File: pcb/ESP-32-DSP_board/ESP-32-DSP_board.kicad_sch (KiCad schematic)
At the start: 65 parts, among them J1 USB_C_Receptacle_USB2.0, J10 Conn_01x01_Pin, J11 Conn_01x01_Pin, J2 Conn_01x04_Pin, J3 Conn_01x04_Pin, J4 Conn_01x07_Pin, J5 Conn_01x07_Pin, J6 Conn_01x01_Pin, J7 Conn_01x01_Pin, J8 Conn_01x01_Pin, J9 Conn_01x01_Pin, Q1 BC847, Q2 BC847, U1 AZ1117IH-3.3, U2 ESP32-WROOM-32UE-N8, U3 USBLC6-2P6, U4 CP2104, U5 ADS8688

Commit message: ESP32-S3 version of dsp board with SD-card and DAC added
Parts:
- removed C11: 4.7u, Capacitor_SMD:C_0603_1608Metric, symbol Device:C
- removed C5: 100n, Capacitor_SMD:C_0402_1005Metric, symbol Device:C
- removed J10, J11, J6, J7, J8, J9: Conn_01x01_Pin, Connector_PinSocket_2.00mm:PinSocket_1x01_P2.00mm_Vertical, symbol Connector:Conn_01x01_Pin
- removed J2, J3: Conn_01x04_Pin, Connector_PinHeader_2.00mm:PinHeader_1x04_P2.00mm_Horizontal, symbol Connector:Conn_01x04_Pin
- removed J4, J5: Conn_01x07_Pin, Connector_PinSocket_2.00mm:PinSocket_1x07_P2.00mm_Vertical, symbol Connector:Conn_01x07_Pin
- removed Q1, Q2: BC847, Package_TO_SOT_SMD:SOT-23, symbol Transistor_BJT:BC847
- removed R10 (x3): 10k, Resistor_SMD:R_0402_1005Metric, symbol Device:R_Small
- removed R10 (x3): 4.7k, Resistor_SMD:R_0402_1005Metric, symbol Device:R_Small
- removed U2: ESP32-WROOM-32UE-N8, RF_Module:ESP32-WROOM-32U, symbol RF_Module:ESP32-WROOM-32U
- removed U4: CP2104, Package_DFN_QFN:QFN-24-1EP_4x4mm_P0.5mm_EP2.6x2.6mm, symbol Interface_USB:CP2104
- added C27, C28: 3.3p, Capacitor_SMD:C_0402_1005Metric, symbol Device:C
- added C29: 10u, Capacitor_SMD:C_0603_1608Metric, symbol Device:C
- added C30: 1u, Capacitor_SMD:C_0603_1608Metric, symbol Device:C
- added C31, C32, C36: 100n, Capacitor_SMD:C_0402_1005Metric, symbol Device:C
- added C33, C34: 12p, Capacitor_SMD:C_0402_1005Metric, symbol Device:C
- added C5: 250u, Capacitor_THT:CP_Radial_D5.0mm_P2.50mm, symbol Device:C_Polarized
- added J12: Conn_Coaxial, Connector_Coaxial:U.FL_Hirose_U.FL-R-SMT-1_Vertical, symbol Connector:Conn_Coaxial
- added J2: Conn_01x10_Pin, Connector_PinHeader_2.54mm:PinHeader_1x10_P2.54mm_Vertical, symbol Connector:Conn_01x10_Pin
- added J5: SD_Card, Connector_Card:microSD_HC_Hirose_DM3D-SF, symbol Connector:SD_Card
- added J6: AudioJack2_Ground, Connector_Audio:Jack_3.5mm_CUI_SJ-3523-SMT_Horizontal, symbol Connector_Audio:AudioJack2_Ground
- added L1, L2, L4: 2.2n, Inductor_SMD:L_0603_1608Metric, symbol Device:L
- added R13: 10k, Resistor_SMD:R_0402_1005Metric, symbol Device:R
- added R14: 10, Resistor_SMD:R_0805_2012Metric, symbol Device:R
- added RV1, RV2: R_Potentiometer, Potentiometer_SMD:Potentiometer_ACP_CA6-VSMD_Vertical, symbol Device:R_Potentiometer
- added U2: AD5689BRUZ, Package_SO:TSSOP-16_4.4x5mm_P0.65mm, symbol Analog_DAC:AD5689BRUZ
- added U4: LM386, Package_SO:SOIC-8_3.9x4.9mm_P1.27mm, symbol Amplifier_Audio:LM386
- added U6: ESP32-S3FH4R2, Package_DFN_QFN:QFN-56-1EP_7x7mm_P0.4mm_EP5.6x5.6mm, symbol PCM_Espressif:ESP32-S3
- added Y1: 40MHz, Crystal:Crystal_SMD_3225-4Pin_3.2x2.5mm, symbol Device:Crystal_GND23
- C1: footprint Capacitor_SMD:C_0805_2012Metric -> Capacitor_SMD:C_0402_1005Metric
- C10: value 4.7u -> 10u
- C7: value 22u -> 10u; footprint Capacitor_SMD:C_0805_2012Metric -> Capacitor_SMD:C_0603_1608Metric
- C8: value 1u -> 10u; footprint Capacitor_SMD:C_0402_1005Metric -> Capacitor_SMD:C_0603_1608Metric
- C9: footprint Capacitor_SMD:C_0402_1005Metric -> Capacitor_SMD:C_0603_1608Metric
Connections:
- net +3.3V: now also C29.1, C30.1, C31.1, J5.4 (VDD), L2.1, R13.1, U2.1 (VREF), U2.10 (GAIN), U2.11 (VLOGIC), U2.15 (~{RESET}), U2.5 (VDD), U2.9 (~{LDAC}), U6.2 (VDD3P3), U6.20 (VDD3P3_RTC), U6.3 (VDD3P3), U6.46 (VDD3P3_CPU), U6.55 (VDDA), U6.56 (VDDA); no longer C7.1
- net ADC_A0: now also J2.3 (Pin_3)
- net ADC_A1: now also J2.4 (Pin_4)
- net ADC_A2: now also J2.5 (Pin_5)
- net ADC_A3: now also J2.6 (Pin_6)
- net ADC_A4: now also J2.7 (Pin_7)
- net ADC_A5: now also J2.8 (Pin_8)
- net ADC_A6: now also J2.1 (Pin_1)
- net ADC_A7: now also J2.2 (Pin_2)
- net ADC_CS: now also U6.9 (GPIO4/ADC1_CH3)
- net ADC_MISO: now also U6.8 (GPIO3/ADC1_CH2)
- net ADC_MOSI: now also U6.7 (GPIO2/ADC1_CH1)
- net ADC_SCLK: now also U6.10 (GPIO5/ADC1_CH4)
- net EN: now also U6.4 (CHIP_PU/RESET); no longer C8.1
- net GND: now also C27.2, C28.2, C29.2, C30.2, C31.2, C32.2, C33.1, C34.1, C36.2, J12.2 (Ext), J5.3 (VSS), J5.6 (VSS), J6.G, U2.16 (RSTSEL), U2.4 (GND), U6.57 (GND), Y1.2, Y1.4; no longer C7.2, C8.2, J1.S1 (SHIELD)
- net GNDA: now also C8.1, J2.9 (Pin_9), RV1.3, RV2.3, U4.2 (-), U4.4 (GND)
- net IO0: now also U6.5 (GPIO0/BOOT)
- net IO16: now also U6.22 (GPIO16/ADC2_CH5/XTAL_32K_N)
- net IO17: now also U6.23 (GPIO17/ADC2_CH6)
- net IO18: now also U6.24 (GPIO18/ADC2_CH7)
- net IO21: now also U6.27 (GPIO21)
- net RX: now also U6.50 (U0RXD/PROG/GPIO44)
- net TX: now also U6.49 (U0TXD/PROG/GPIO43)
- net USB_D+: now also U6.26 (GPIO20/USB_D+/ADC2_CH9)
- net USB_D-: now also U6.25 (GPIO19/USB_D-/ADC2_CH8)
- net VBUS renamed +5V
- net +5V: now also J2.10 (Pin_10), L4.1, U4.6 (V+); no longer C2.1, U1.3 (VI), U3.5 (VBUS)
- new net: C32.1, L2.2
- new net: C2.1, C36.1, L4.2, U1.3 (VI), U3.5 (VBUS)
- new net: C28.1, J12.1 (In), L1.1
- new net: C27.1, L1.2, U6.1 (LNA_IN/RF)
- new net: C33.2, U6.53 (XTAL_N), Y1.3
- new net: R14.1, U6.54 (XTAL_P)
- new net: RV2.1, U4.1 (GAIN)
- new net: C7.2, RV2.2
- new net: C34.2, R14.2, Y1.1
- new net: C5.1, U4.5
- new net: C5.2, J6.S, J6.T
- new net: C7.1, U4.8 (GAIN)
- new net: RV1.1, U2.3 (VOUTA)
- new net: RV1.2, U4.3 (+)
- new net: C8.2, U4.7 (BYPASS)
- new net DAC_MISO: U2.14 (SDIN), U6.15 (GPIO10/ADC1_CH9)
- new net DAC_MOSI: U2.8 (SDO), U6.18 (GPIO13/ADC2_CH2)
- new net DAC_SCLK: U2.12 (SCLK), U6.17 (GPIO12/ADC2_CH1)
- new net DAC_SYNC: U2.13 (~{SYNC}), U6.16 (GPIO11/ADC2_CH0)
- new net IO1: U6.6 (GPIO1/ADC1_CH0)
- new net IO14: U6.19 (GPIO14/ADC2_CH3)
- new net IO15: U6.21 (GPIO15/ADC2_CH4/XTAL_32K_P)
- new net IO38: U6.43 (GPIO38)
- new net IO39: U6.44 (MTCK/JTAG/GPIO39)
- new net IO40: U6.45 (MTDO/JTAG/GPIO40)
- new net IO41: U6.47 (MTDI/JTAG/GPIO41)
- new net IO42: U6.48 (MTMS/JTAG/GPIO42)
- new net IO45: R13.2, U6.51 (GPIO45)
- new net IO46: U6.52 (GPIO46)
- new net IO47: U6.37 (SPICLK_P/GPIO47)
- new net IO48: U6.36 (SPICLK_N/GPIO48)
- new net SD_CS: J5.1 (CD/DAT3), U6.11 (GPIO6/ADC1_CH5)
- new net SD_MISO: J5.7 (DAT0), U6.14 (GPIO9/ADC1_CH8)
- new net SD_MOSI: J5.2 (CMD), U6.12 (GPIO7/ADC1_CH6)
- new net SD_SCLK: J5.5 (CLK), U6.13 (GPIO8/ADC1_CH7)
- no-connect marks 20 -> 16
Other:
- note added: "ADC connector pins"
- note added: "Boot KEEP IO0 FREE"
- note added: "Check for correct crustal"
- note added: "DAC - Audio output"
- note added: "ESP - wifi/bluetooth antenna"
- note added: "IO-pins"
- note added: "Internal ram and flash"
- note added: "MCU - ESP32-S3"
- note added: "SD-Card"
- note added: "USB, power delivert and static protection"
- note removed: "ADC analog pins"
- note removed: "Auto porgram"
- note removed: "ESP GPIO-Headers"
- note removed: "If model has ESP-32_D0WDR2-V3 Pull IO16 to 3.3v"
- note removed: "MCU - ESP32-WROOM-U"
- note removed: "USB"
- note removed: "USB-UART Bridge - CP2104"
- moved on the sheet: C1, C12, C13, C14, C15, C16, C17, C18, C19, C2, C20, C21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

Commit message: First working version of S3 dsp board
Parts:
- removed J6: AudioJack2_Ground, Connector_Audio:Jack_3.5mm_CUI_SJ-3523-SMT_Horizontal, symbol Connector_Audio:AudioJack2_Ground
- added J3: AudioJack2_Ground, Connector_Audio:Jack_3.5mm_CUI_SJ-3523-SMT_Horizontal, symbol Connector_Audio:AudioJack2_Ground
- added J4, J6, J7: Conn_01x08_Pin, Connector_PinHeader_2.54mm:PinHeader_1x08_P2.54mm_Vertical, symbol Connector:Conn_01x08_Pin
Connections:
- net +3.3V: now also U6.29 (VDD_SPI), J4.2 (Pin_2), J6.2 (Pin_2), J7.2 (Pin_2)
- net +5V: now also J4.3 (Pin_3), J6.3 (Pin_3), J7.3 (Pin_3)
- net GND: now also J5.10 (CARD_DETECT), J5.11 (WRITE_PROTECT), J4.1 (Pin_1), J6.1 (Pin_1), J7.1 (Pin_1)
- net GNDA: now also J3.R
- net IO14: now also J6.8 (Pin_8)
- net IO15: now also J6.6 (Pin_6)
- net IO16: now also J6.5 (Pin_5)
- net IO17: now also J6.7 (Pin_7)
- net IO18: now also J4.4 (Pin_4)
- net IO21: now also J4.5 (Pin_5)
- net IO38: now also J4.8 (Pin_8)
- net IO39: now also J7.8 (Pin_8)
- net IO40: now also J7.7 (Pin_7)
- net IO41: now also J7.6 (Pin_6)
- net IO42: now also J7.5 (Pin_5)
- net IO46: now also J7.4 (Pin_4)
- net IO47: now also J4.7 (Pin_7)
- net IO48: now also J4.6 (Pin_6)
- net ADC_REF_CAP: now reaches C12.2, C16.1, C17.1, U5.7 (REFCAP)
- net at C5.2: now also J3.S, J3.T

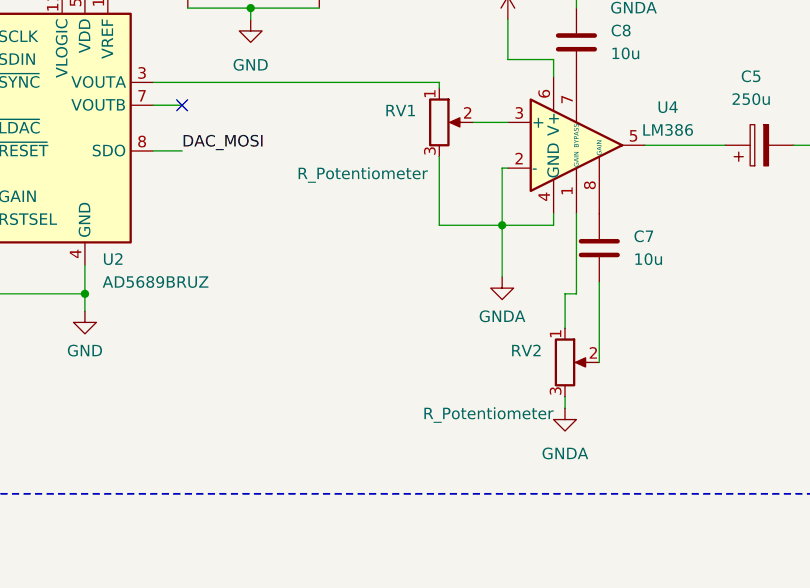
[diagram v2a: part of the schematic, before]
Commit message: ESP32-S3 DSP updates
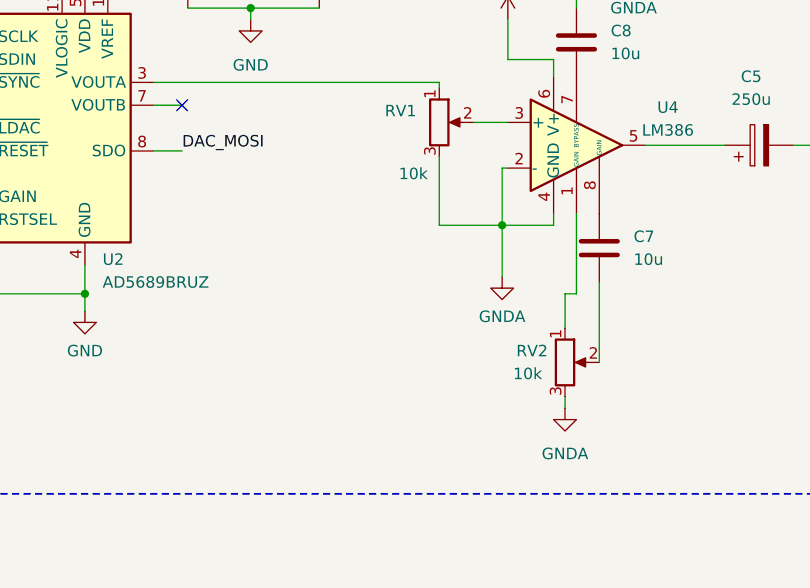
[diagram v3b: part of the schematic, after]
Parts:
- RV1, RV2: value R_Potentiometer -> 10k; footprint Potentiometer_SMD:Potentiometer_ACP_CA6-VSMD_Vertical -> Potentiometer_SMD:Potentiometer_Bourns_3214J_Horizontal
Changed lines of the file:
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@@
   (symbol (lib_id "Device:R_Potentiometer") (at 332.74 238.76 0) (unit 1)
     (in_bom yes) (on_board yes) (dnp no)
-    (property "Reference" "RV2" (at 330.2 237.49 0)
+    (property "Reference" "RV2" (at 330.835 237.49 0)
       (effects (font (size 1.27 1.27)) (justify right))
     )
-    (property "Value" "R_Potentiometer" (at 331.47 244.475 0)
+    (property "Value" "10k" (at 330.2 240.03 0)
       (effects (font (size 1.27 1.27)) (justify right))
     )
-    (property "Footprint" "Potentiometer_SMD:Potentiometer_ACP_CA6-VSMD_Vertical" (at 332.74 238.76 0)
+    (property "Footprint" "Potentiometer_SMD:Potentiometer_Bourns_3214J_Horizontal" (at 332.74 238.76 0)
       (effects (font (size 1.27 1.27)) hide)
     )
@@
       (effects (font (size 1.27 1.27)) (justify right))
     )
-    (property "Value" "R_Potentiometer" (at 317.5 217.805 0)
+    (property "Value" "10k" (at 317.5 217.805 0)
       (effects (font (size 1.27 1.27)) (justify right))
     )
-    (property "Footprint" "Potentiometer_SMD:Potentiometer_ACP_CA6-VSMD_Vertical" (at 318.77 212.09 0)
-      (effects (font (size 1.27 1.27)) hide)
-    )
+    (property "Footprint" "Potentiometer_SMD:Potentiometer_Bourns_3214J_Horizontal" (at 318.77 212.09 0)
+      (effects (font (size 1.27 1.27)) hide)
+    )

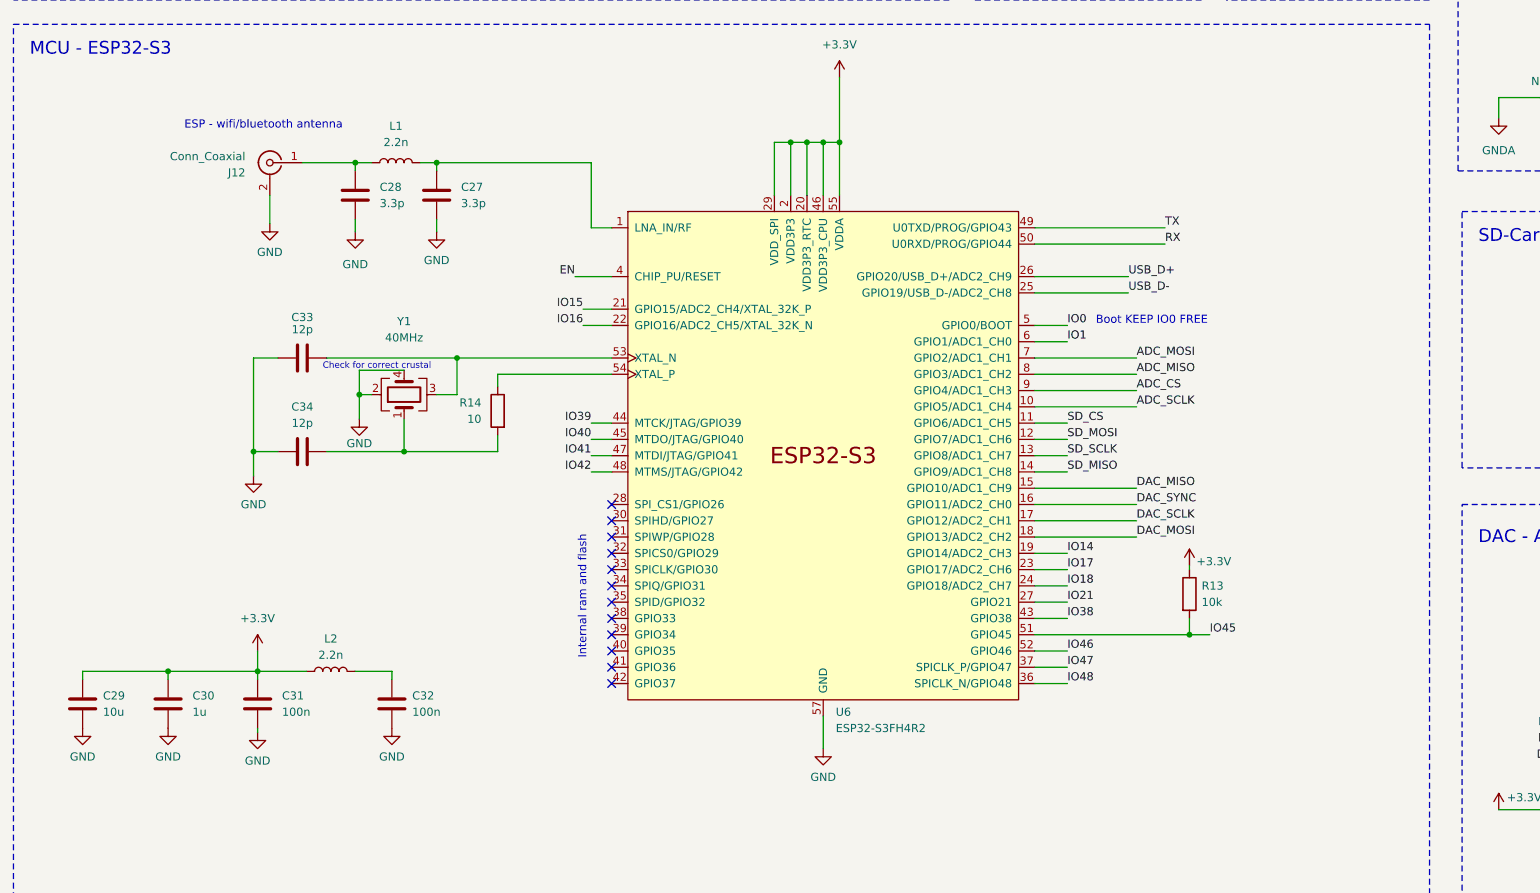
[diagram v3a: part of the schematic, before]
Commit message: Fixed mistake in S3 dsp
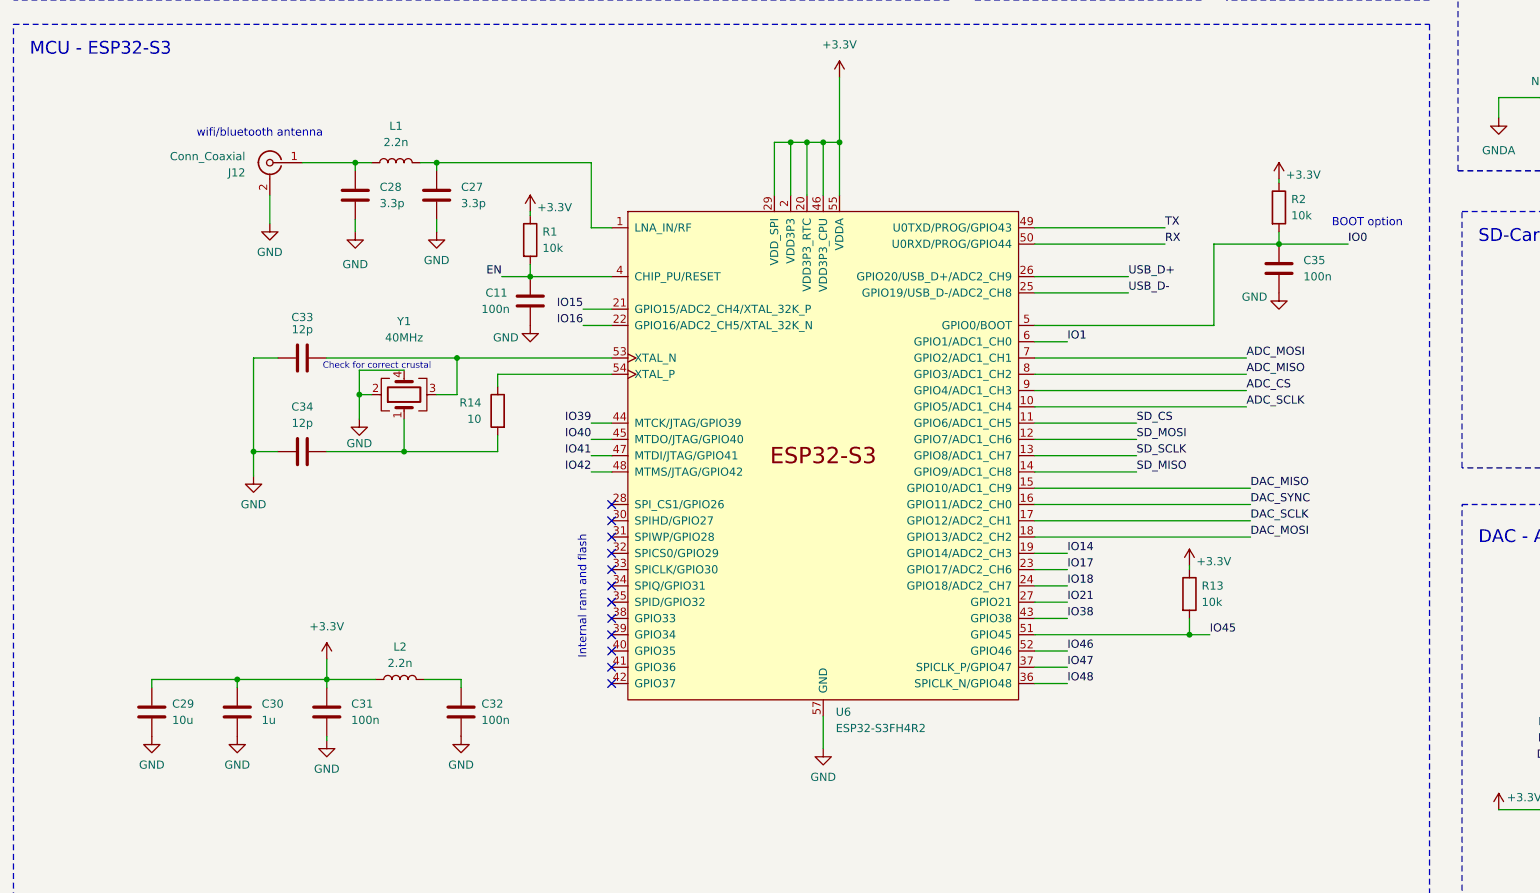
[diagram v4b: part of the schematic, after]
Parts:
- added C11, C35: 100n, Capacitor_SMD:C_0402_1005Metric, symbol Device:C
- added R1, R2: 10k, Resistor_SMD:R_0402_1005Metric, symbol Device:R
- J3: footprint Connector_Audio:Jack_3.5mm_CUI_SJ-3523-SMT_Horizontal -> Connector_Audio:Jack_3.5mm_CUI_SJ-3524-SMT_Horizontal
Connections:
- net +3.3V: now also R1.1, R2.1
- net EN: now also C11.1, R1.2
- net GND: now also C11.2, C35.2
- net IO0: now also C35.1, R2.2
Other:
- note added: "BOOT option"
- note added: "wifi/bluetooth antenna"
- note removed: "Boot KEEP IO0 FREE"
- note removed: "ESP - wifi/bluetooth antenna"
- moved on the sheet: C29, C30, C31, C32, L2
